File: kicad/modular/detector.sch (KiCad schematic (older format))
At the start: 20 parts, among them J3 HEADER, U3 OPA4197, U4 REF5010

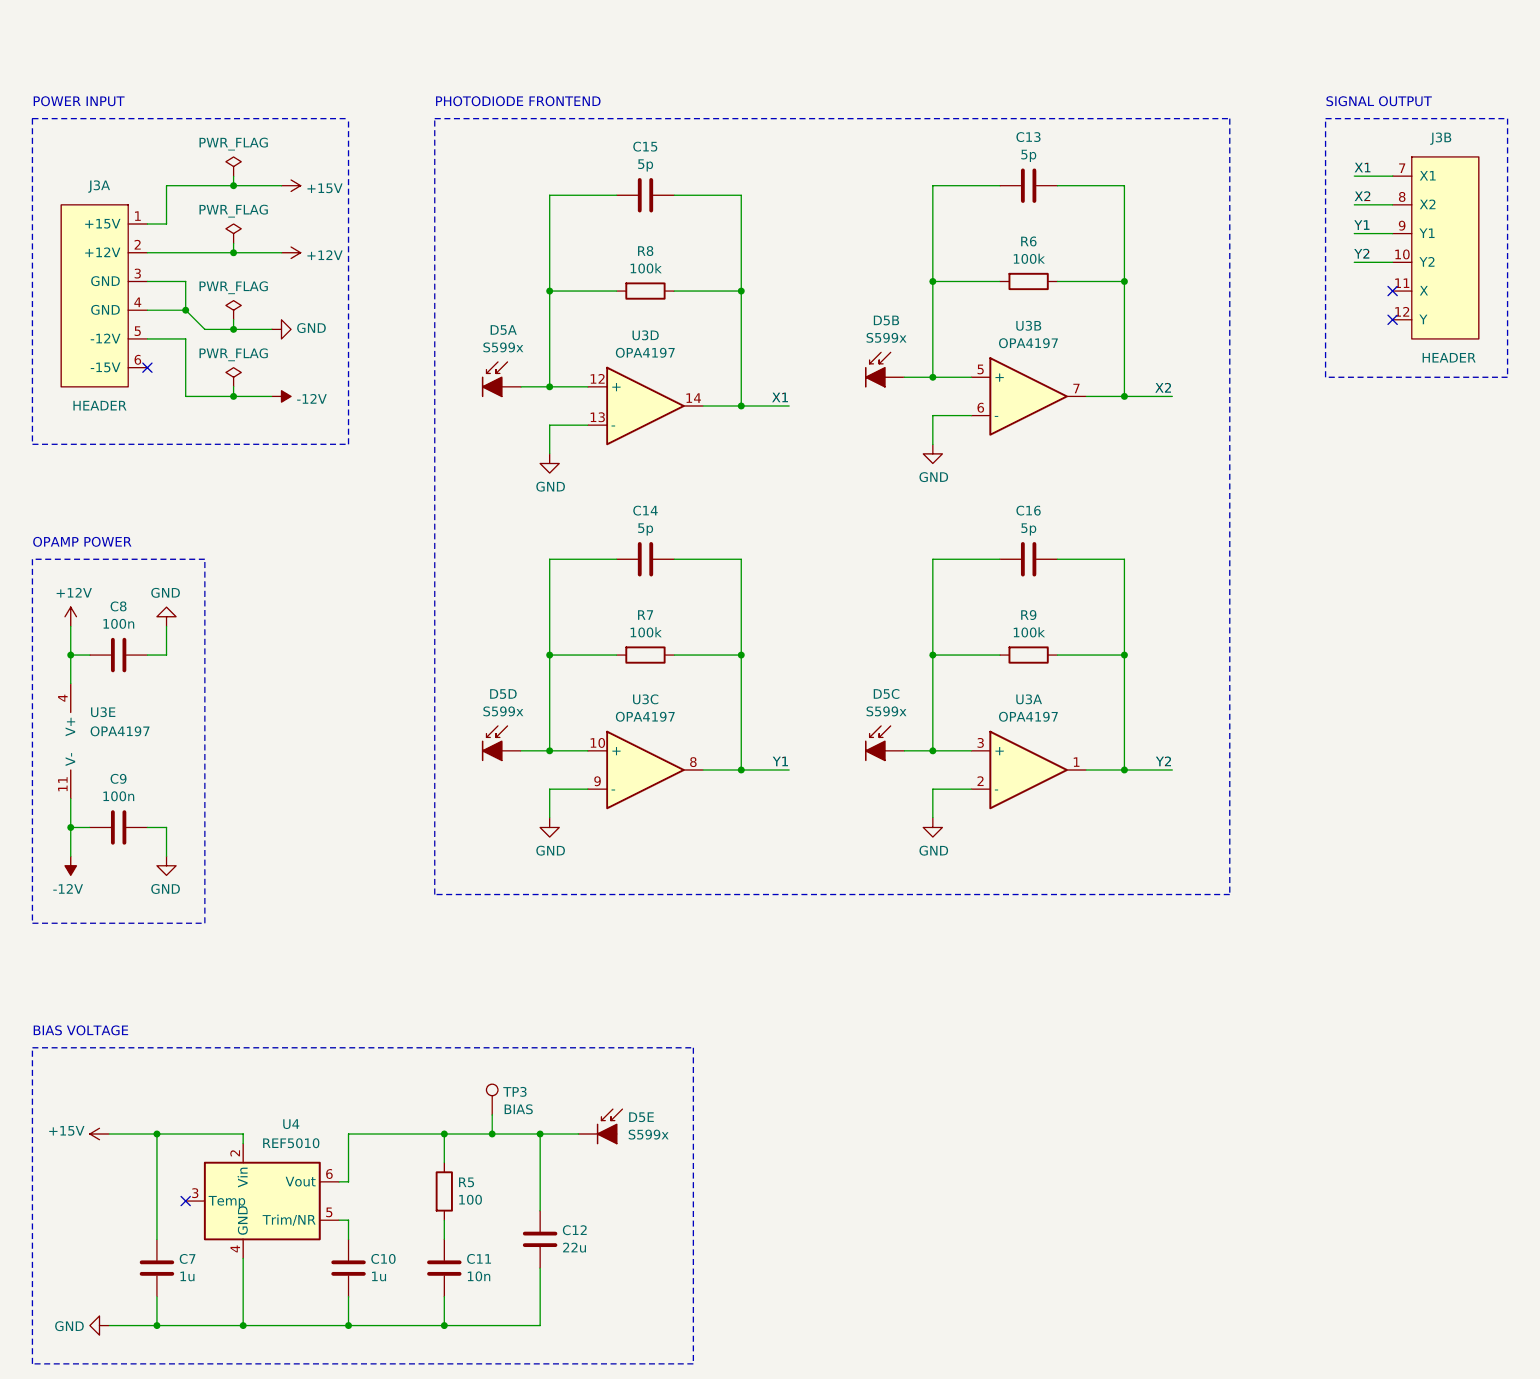
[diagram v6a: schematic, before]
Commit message: applied pcb design suggestions to modular boards
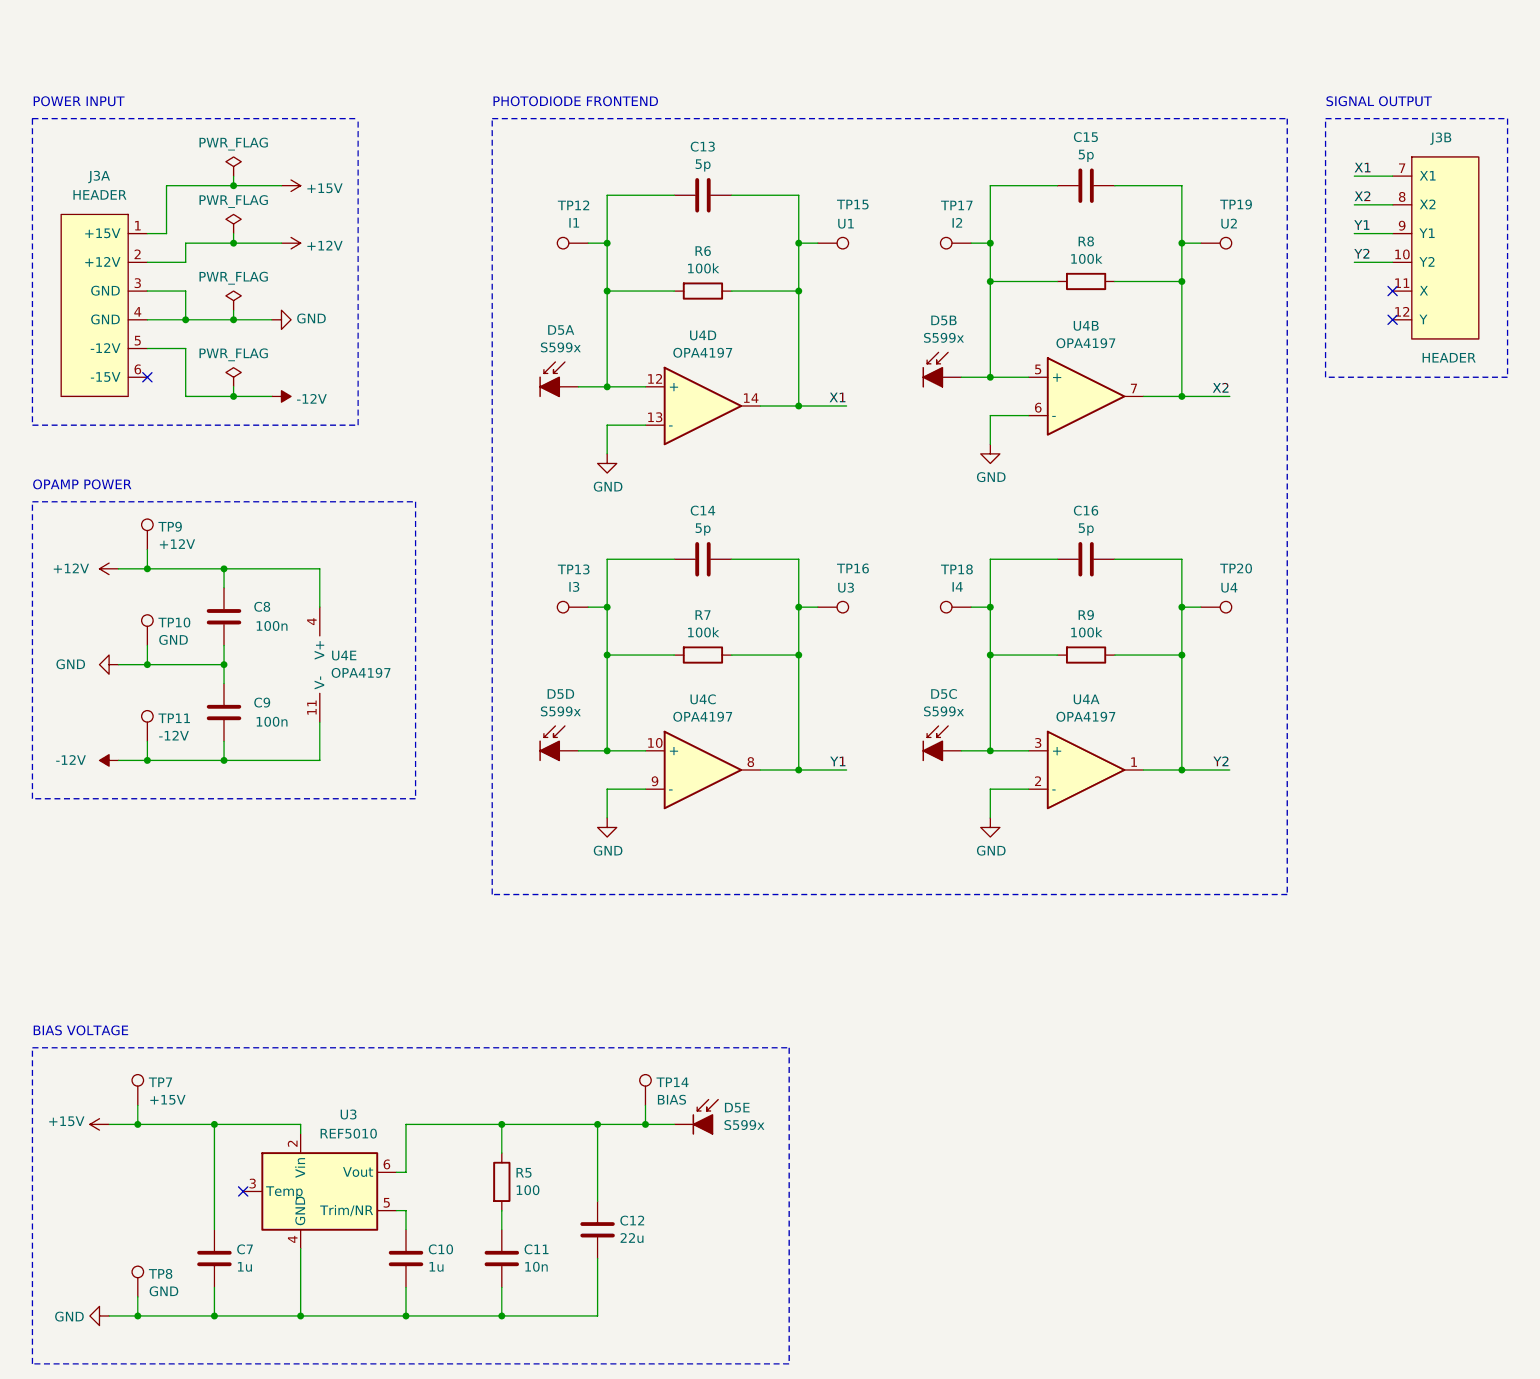
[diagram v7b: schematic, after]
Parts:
- removed unit 5 of U3
- added TP10, TP8: GND, TestPoint:TestPoint_THTPad_D1.0mm_Drill0.5mm, symbol Connector:TestPoint
- added TP11: -12V, TestPoint:TestPoint_THTPad_D1.0mm_Drill0.5mm, symbol Connector:TestPoint
- added TP12: I1, TestPoint:TestPoint_THTPad_D1.0mm_Drill0.5mm, symbol Connector:TestPoint
- added TP13: I3, TestPoint:TestPoint_THTPad_D1.0mm_Drill0.5mm, symbol Connector:TestPoint
- added TP15: U1, TestPoint:TestPoint_THTPad_D1.0mm_Drill0.5mm, symbol Connector:TestPoint
- added TP16: U3, TestPoint:TestPoint_THTPad_D1.0mm_Drill0.5mm, symbol Connector:TestPoint
- added TP17: I2, TestPoint:TestPoint_THTPad_D1.0mm_Drill0.5mm, symbol Connector:TestPoint
- added TP18: I4, TestPoint:TestPoint_THTPad_D1.0mm_Drill0.5mm, symbol Connector:TestPoint
- added TP19: U2, TestPoint:TestPoint_THTPad_D1.0mm_Drill0.5mm, symbol Connector:TestPoint
- added TP20: U4, TestPoint:TestPoint_THTPad_D1.0mm_Drill0.5mm, symbol Connector:TestPoint
- added TP7: +15V, TestPoint:TestPoint_THTPad_D1.0mm_Drill0.5mm, symbol Connector:TestPoint
- added TP9: +12V, TestPoint:TestPoint_THTPad_D1.0mm_Drill0.5mm, symbol Connector:TestPoint
- added unit 5 of U4
- renumbered C15 to C13, C13 to C15, R8 to R6, R6 to R8, TP3 to TP14, U4 to U3, U3 to U4
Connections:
- net +12V: now also TP9.1, U4.4 (V+)
- net +15V: now also TP7.1
- net -12V: now also C9.1, TP11.1, U4.11 (V-); no longer C9.2
- net GND: now also C9.2, TP10.1, TP8.1; no longer C9.1
- net X1: now also TP15.1
- net X2: now also TP19.1
- net Y1: now also TP16.1
- net Y2: now also TP20.1
- net at C13.2, D5.1 (I1), R6.2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: now also TP12.1
- net at C15.2, D5.6 (I2), R8.2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: now also TP17.1
- net at C14.2, D5.5 (I3), R7.2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: now also TP13.1
- net at C16.2, D5.10 (I4), R9.2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: now also TP18.1
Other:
- moved on the sheet: C10, C11, C12, C13, C14, C15, C16, C7, C8, C9, D5A, D5B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

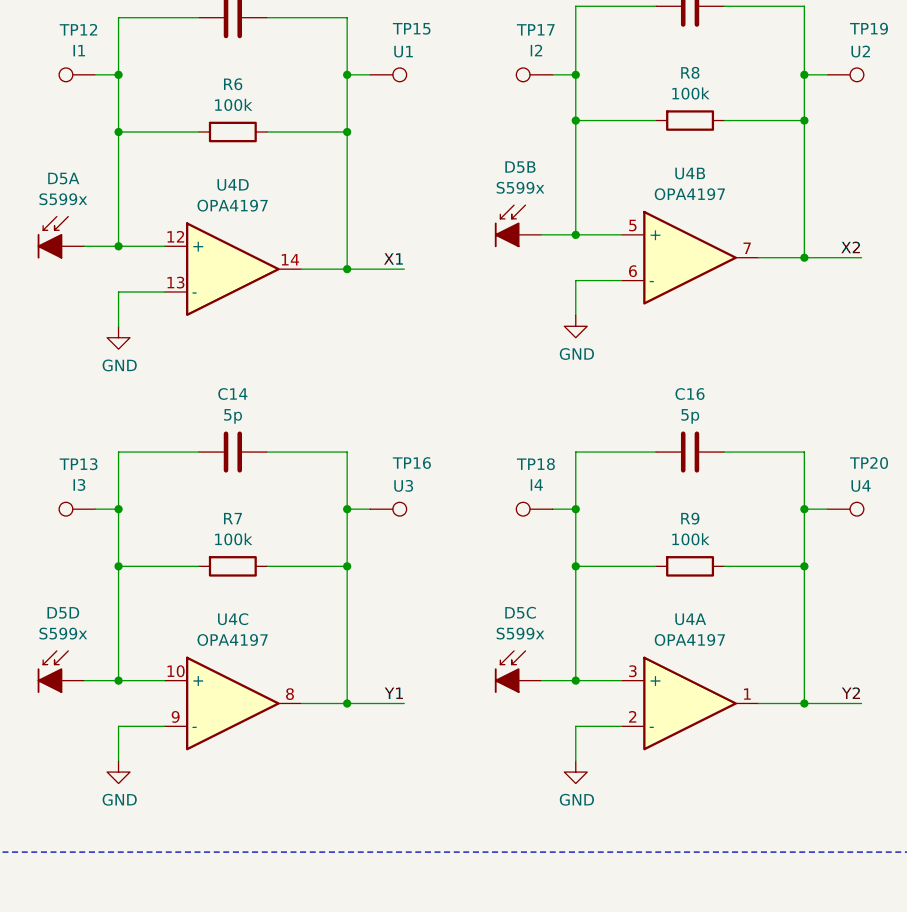
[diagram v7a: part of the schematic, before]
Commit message: fixed opamp input terminal connection, connected some caps directly to gnd through vias
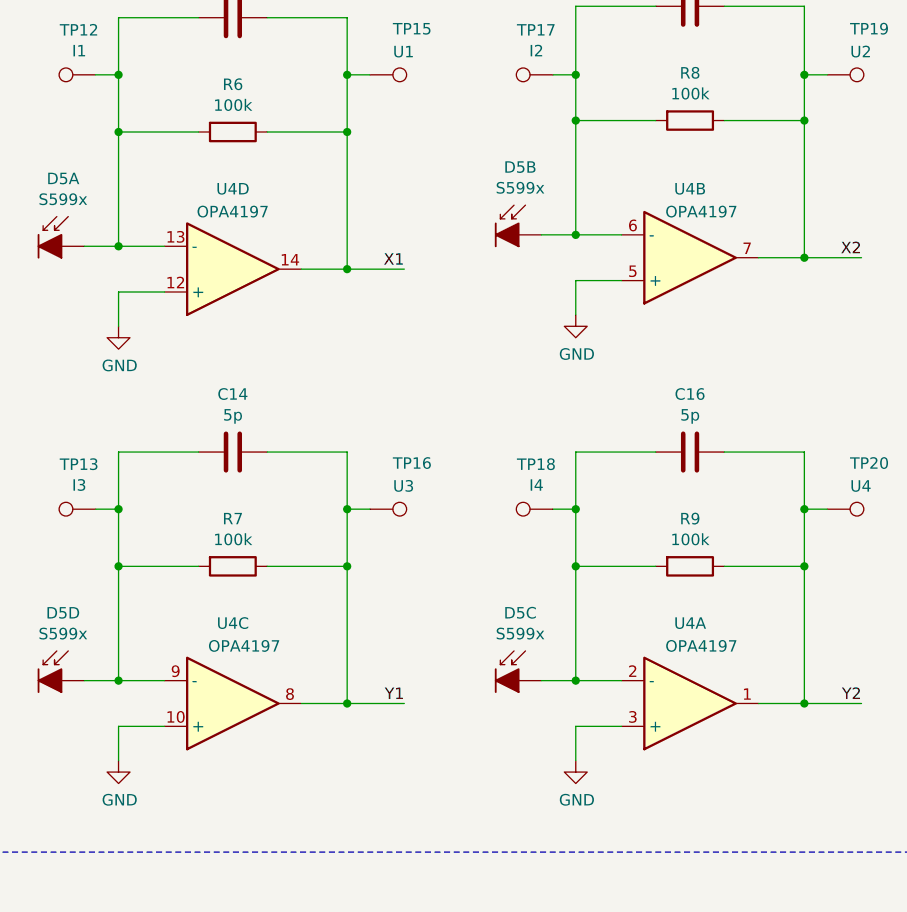
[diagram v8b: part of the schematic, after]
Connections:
- net GND: now also U4.10 (+), U4.12 (+), U4.3 (+), U4.5 (+); no longer U4.13 (-), U4.2 (-), U4.6 (-), U4.9 (-)
- net at C13.2, D5.1 (I1), R6.2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: now also U4.13 (-); no longer U4.12 (+)
- net at C15.2, D5.6 (I2), R8.2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: now also U4.6 (-); no longer U4.5 (+)
- net at C14.2, D5.5 (I3), R7.2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: now also U4.9 (-); no longer U4.10 (+)
- net at C16.2, D5.10 (I4), R9.2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: now also U4.2 (-); no longer U4.3 (+)
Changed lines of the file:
@@
 U 2 1 5D4E6F20
 P 7200 2450
-F 0 "U4" H 7200 2817 50  0000 C CNN
-F 1 "OPA4197" H 7200 2726 50  0000 C CNN
+F 0 "U4" H 7200 2150 50  0000 C CNN
+F 1 "OPA4197" H 7250 2250 50  0000 C CNN
 F 2 "Package_SO:TSSOP-14_4.4x5mm_P0.65mm" H 7200 2450 50  0001 C CNN
 F 3 "~" H 7200 2450 50  0001 C CNN
 	2    7200 2450
-	1    0    0    -1
+	1    0    0    1
 $EndComp
 Wire Wire Line
@@
 U 4 1 5D4FB443
 P 5200 2500
-F 0 "U4" H 5200 2867 50  0000 C CNN
-F 1 "OPA4197" H 5200 2776 50  0000 C CNN
+F 0 "U4" H 5200 2150 50  0000 C CNN
+F 1 "OPA4197" H 5200 2250 50  0000 C CNN
 F 2 "Package_SO:TSSOP-14_4.4x5mm_P0.65mm" H 5200 2500 50  0001 C CNN
 F 3 "~" H 5200 2500 50  0001 C CNN
 	4    5200 2500
-	1    0    0    -1
+	1    0    0    1
 $EndComp
 Wire Wire Line
@@
 U 3 1 5D50785D
 P 5200 4400
-F 0 "U4" H 5200 4767 50  0000 C CNN
-F 1 "OPA4197" H 5200 4676 50  0000 C CNN
+F 0 "U4" H 5200 4050 50  0000 C CNN
+F 1 "OPA4197" H 5250 4150 50  0000 C CNN
 F 2 "Package_SO:TSSOP-14_4.4x5mm_P0.65mm" H 5200 4400 50  0001 C CNN
 F 3 "~" H 5200 4400 50  0001 C CNN
 	3    5200 4400
-	1    0    0    -1
+	1    0    0    1
 $EndComp
 $Comp
@@
 U 1 1 5D50871E
 P 7200 4400
-F 0 "U4" H 7200 4767 50  0000 C CNN
-F 1 "OPA4197" H 7200 4676 50  0000 C CNN
+F 0 "U4" H 7200 4050 50  0000 C CNN
+F 1 "OPA4197" H 7250 4150 50  0000 C CNN
 F 2 "Package_SO:TSSOP-14_4.4x5mm_P0.65mm" H 7200 4400 50  0001 C CNN
 F 3 "~" H 7200 4400 50  0001 C CNN
 	1    7200 4400
-	1    0    0    -1
-$EndComp
-$Comp
+	1    0    0    1
+$EndComp
+$Comp
